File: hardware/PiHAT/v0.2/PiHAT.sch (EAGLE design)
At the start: 41 parts, among them U1 ATMEGA328P, U2 TSL2561, U3 OPA344, U4 MPL115A, U6 ADMP401, U7 SHT31-DIS, Y1 16MHZ

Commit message: Updated PiAQ HAT to v0.2
- Added LEDs on GPIO 05, 26
- Replaced IAQ Core with CCS811
- Added more thermal isolation and rerouted traces
- Minor silkscreen adjustments
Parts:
- removed IAQ-CORE: IAQ-CORE, IAQ-CORE:IAQ-CORE
- added LED_05, LED_26: (no value), adafruit:LEDCHIPLED_0805
- added R10, R2: 47, SparkFun-Resistors:RESISTOR0805-RES
- added R9: 100K, SparkFun-Passives:RESISTOR0805-RES
- added U$1: CCS811, CCS811:CCS811-I2C
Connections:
- new net N$1: LED_26.A, R2.1
- new net N$16: R9.2, U$1.ADDR
- new net N$6: LED_05.A, R10.1
- net GND: now also LED_05.C, LED_26.C, U$1.GND; no longer IAQ-CORE.GND
- net GPIO26: now also R2.2
- net GPIO5: now also R10.2
- net SCL: now also U$1.SCL; no longer IAQ-CORE.SCL
- net SDA: now also U$1.SDA; no longer IAQ-CORE.SDA
- net VCC: now also R9.1, U$1.VDD; no longer IAQ-CORE.VCC
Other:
- note added: "0x5B"
- note added: "v0.2 (October 2016)"
- note removed: "0x5A"
- note removed: "v0.1 (September 2016)"
- moved on the sheet: C5

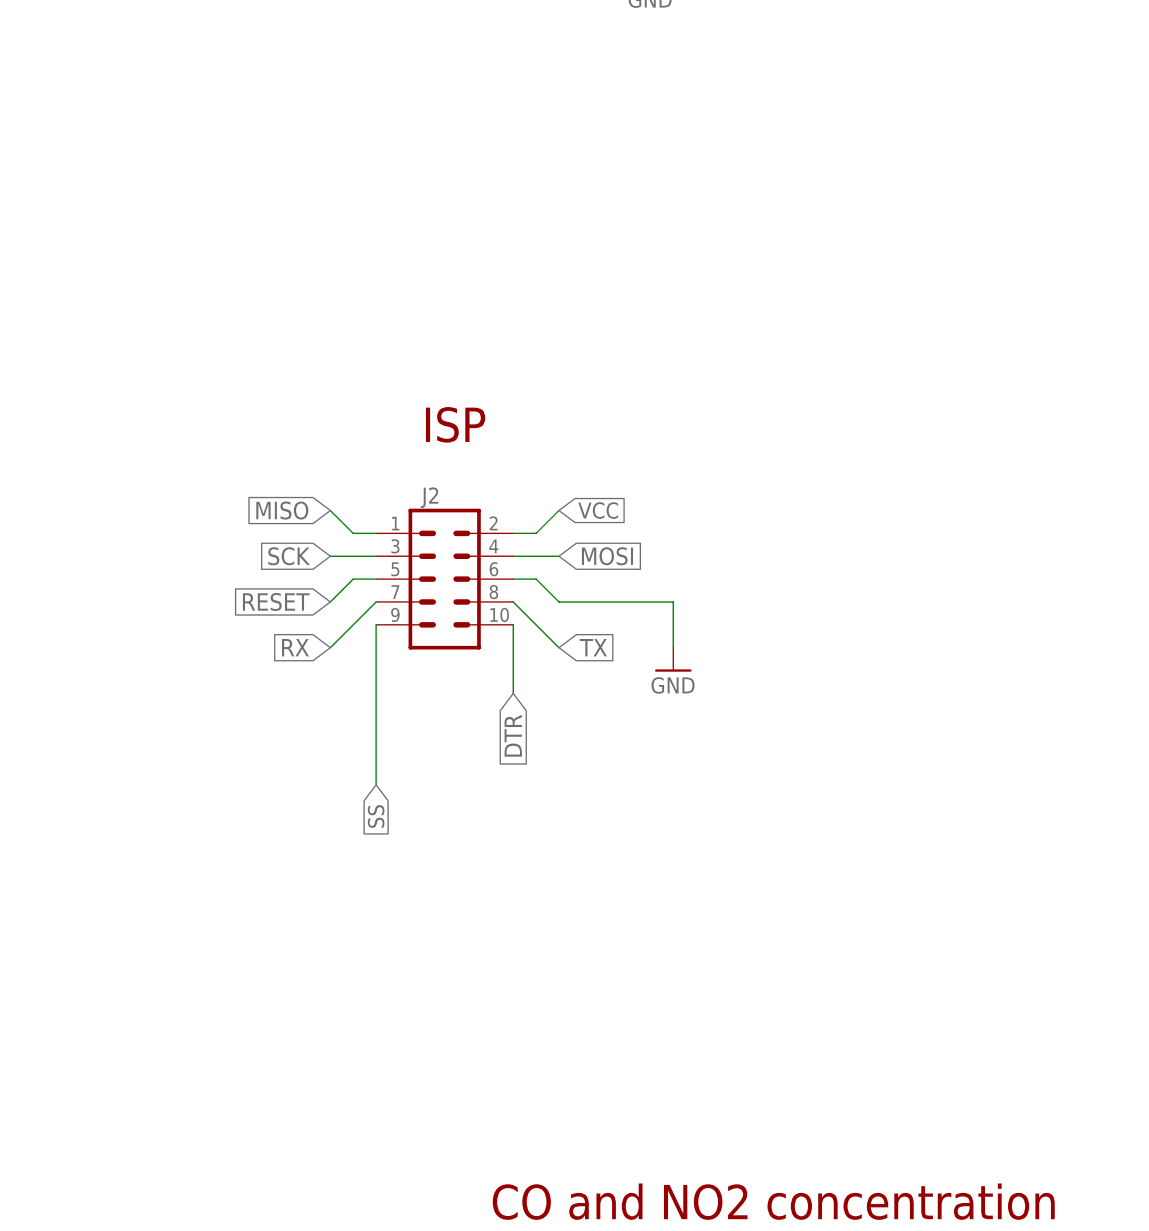
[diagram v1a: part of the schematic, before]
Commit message: Minor fixes to sensor board v0.6
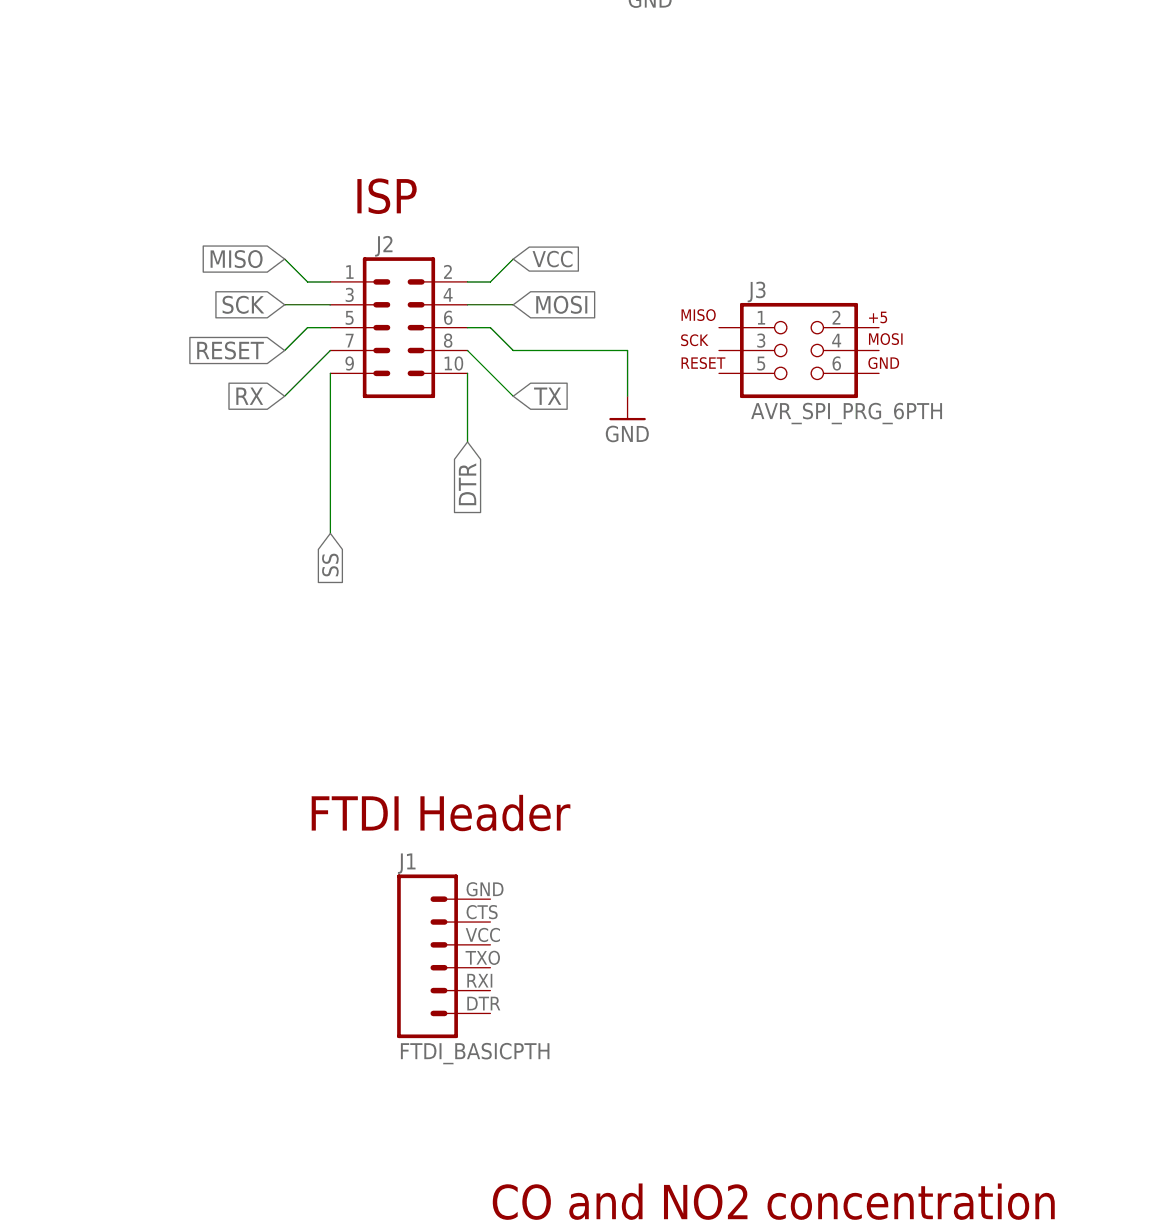
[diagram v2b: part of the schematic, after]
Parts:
- added J1: FTDI_BASICPTH, SparkFun-Connectors:FTDI_BASICPTH
- added J3: AVR_SPI_PRG_6PTH, SparkFun-Connectors:AVR_SPI_PRG_6PTH
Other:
- note added: "FTDI Header"
- moved on the sheet: J2
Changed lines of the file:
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@@
 <attribute name="OC_NEWARK" value="unknown"/>
 </part>
+<part name="J1" library="SparkFun-Connectors" deviceset="FTDI_BASIC" device="PTH"/>
+<part name="J3" library="SparkFun-Connectors" deviceset="AVR_SPI_PRG_6" device="PTH"/>
 </parts>
 <sheets>
@@
 <text x="447.04" y="-71.12" size="3.81" layer="94">Sound Intensity</text>
 <text x="426.72" y="17.78" size="3.81" layer="94">Temperature and Relative Humidity</text>
-<text x="185.42" y="5.08" size="3.81" layer="94">ISP</text>
+<text x="177.8" y="30.48" size="3.81" layer="94">ISP</text>
 <text x="193.04" y="-81.28" size="3.81" layer="94">CO and NO2 concentration</text>
 <text x="322.58" y="-132.08" size="5.08" layer="94" font="vector" ratio="20">CRT Labs</text>
@@
 <text x="467.36" y="-17.78" size="1.778" layer="97">0x44</text>
 <frame x1="104.14" y1="-167.64" x2="568.96" y2="165.1" columns="8" rows="5" layer="94"/>
+<text x="172.72" y="-38.1" size="3.81" layer="94">FTDI Header</text>
 </plain>
 <instances>
@@
 </instance>
 <instance part="SUPPLY11" gate="G$1" x="426.72" y="132.08"/>
-<instance part="J2" gate="G$1" x="187.96" y="-10.16">
-<attribute name="DIGIKEY#" x="187.96" y="-10.16" size="1.778" layer="96" display="off"/>
+<instance part="J2" gate="G$1" x="182.88" y="17.78">
+<attribute name="DIGIKEY#" x="182.88" y="17.78" size="1.778" layer="96" display="off"/>
 </instance>
 <instance part="U4" gate="G$1" x="325.12" y="109.22">
@@
 </instance>
 <instance part="SUPPLY12" gate="G$1" x="289.56" y="119.38"/>
-<instance part="GND6" gate="1" x="213.36" y="-20.32"/>
+<instance part="GND6" gate="1" x="208.28" y="7.62"/>
 <instance part="MICS4514" gate="G$1" x="254" y="-99.06"/>
 <instance part="R14" gate="G$1" x="223.52" y="-111.76" rot="R90">
@@
 <attribute name="DIGIKEY#" x="129.54" y="73.66" size="1.778" layer="96" rot="R270" display="off"/>
 </instance>
+<instance part="J1" gate="G$1" x="187.96" y="-53.34"/>
+<instance part="J3" gate="G$1" x="226.06" y="15.24"/>
 </instances>
 <busses>
@@
 <segment>
 <pinref part="J2" gate="G$1" pin="6"/>
-<wire x1="195.58" y1="-10.16" x2="198.12" y2="-10.16" width="0.1524" layer="91"/>
-<wire x1="198.12" y1="-10.16" x2="200.66" y2="-12.7" width="0.1524" layer="91"/>
-<wire x1="200.66" y1="-12.7" x2="213.36" y2="-12.7" width="0.1524" layer="91"/>
-<wire x1="213.36" y1="-12.7" x2="213.36" y2="-17.78" width="0.1524" layer="91"/>
+<wire x1="190.5" y1="17.78" x2="193.04" y2="17.78" width="0.1524" layer="91"/>
+<wire x1="193.04" y1="17.78" x2="195.58" y2="15.24" width="0.1524" layer="91"/>
+<wire x1="195.58" y1="15.24" x2="208.28" y2="15.24" width="0.1524" layer="91"/>
+<wire x1="208.28" y1="15.24" x2="208.28" y2="10.16" width="0.1524" layer="91"/>
 <pinref part="GND6" gate="1" pin="GND"/>
 </segment>
@@
 <segment>
 <pinref part="J2" gate="G$1" pin="2"/>
-<wire x1="195.58" y1="-5.08" x2="198.12" y2="-5.08" width="0.1524" layer="91"/>
-<wire x1="198.12" y1="-5.08" x2="200.66" y2="-2.54" width="0.1524" layer="91"/>
-<label x="200.66" y="-2.54" size="1.778" layer="95" xref="yes"/>
+<wire x1="190.5" y1="22.86" x2="193.04" y2="22.86" width="0.1524" layer="91"/>
+<wire x1="193.04" y1="22.86" x2="195.58" y2="25.4" width="0.1524" layer="91"/>
+<label x="195.58" y="25.4" size="1.778" layer="95" xref="yes"/>
 </segment>
 <segment>
@@
 <segment>
 <pinref part="J2" gate="G$1" pin="1"/>
-<wire x1="180.34" y1="-5.08" x2="177.8" y2="-5.08" width="0.1524" layer="91"/>
-<wire x1="177.8" y1="-5.08" x2="175.26" y2="-2.54" width="0.1524" layer="91"/>
-<label x="175.26" y="-2.54" size="1.9304" layer="95" rot="R180" xref="yes"/>
+<wire x1="175.26" y1="22.86" x2="172.72" y2="22.86" width="0.1524" layer="91"/>
+<wire x1="172.72" y1="22.86" x2="170.18" y2="25.4" width="0.1524" layer="91"/>
+<label x="170.18" y="25.4" size="1.9304" layer="95" rot="R180" xref="yes"/>
 </segment>
 </net>
@@
 <segment>
 <pinref part="J2" gate="G$1" pin="3"/>
-<wire x1="180.34" y1="-7.62" x2="175.26" y2="-7.62" width="0.1524" layer="91"/>
-<label x="175.26" y="-7.62" size="1.9304" layer="95" rot="R180" xref="yes"/>
+<wire x1="175.26" y1="20.32" x2="170.18" y2="20.32" width="0.1524" layer="91"/>
+<label x="170.18" y="20.32" size="1.9304" layer="95" rot="R180" xref="yes"/>
 </segment>
 </net>
@@
 <segment>
 <pinref part="J2" gate="G$1" pin="5"/>
-<wire x1="180.34" y1="-10.16" x2="177.8" y2="-10.16" width="0.1524" layer="91"/>
-<wire x1="177.8" y1="-10.16" x2="175.26" y2="-12.7" width="0.1524" layer="91"/>
-<label x="175.26" y="-12.7" size="1.9304" layer="95" rot="R180" xref="yes"/>
+<wire x1="175.26" y1="17.78" x2="172.72" y2="17.78" width="0.1524" layer="91"/>
+<wire x1="172.72" y1="17.78" x2="170.18" y2="15.24" width="0.1524" layer="91"/>
+<label x="170.18" y="15.24" size="1.9304" layer="95" rot="R180" xref="yes"/>
 </segment>
 </net>
@@
 <segment>
 <pinref part="J2" gate="G$1" pin="4"/>
-<wire x1="195.58" y1="-7.62" x2="200.66" y2="-7.62" width="0.1524" layer="91"/>
-<label x="200.66" y="-7.62" size="1.9304" layer="95" xref="yes"/>
+<wire x1="190.5" y1="20.32" x2="195.58" y2="20.32" width="0.1524" layer="91"/>
+<label x="195.58" y="20.32" size="1.9304" layer="95" xref="yes"/>
 </segment>
 </net>
@@
 <segment>
 <pinref part="J2" gate="G$1" pin="10"/>
-<wire x1="195.58" y1="-15.24" x2="195.58" y2="-22.86" width="0.1524" layer="91"/>
-<label x="195.58" y="-22.86" size="1.9304" layer="95" rot="R270" xref="yes"/>
+<wire x1="190.5" y1="12.7" x2="190.5" y2="5.08" width="0.1524" layer="91"/>
+<label x="190.5" y="5.08" size="1.9304" layer="95" rot="R270" xref="yes"/>
 </segment>
 </net>
@@
 <segment>
 <pinref part="J2" gate="G$1" pin="7"/>
-<wire x1="180.34" y1="-12.7" x2="175.26" y2="-17.78" width="0.1524" layer="91"/>
-<label x="175.26" y="-17.78" size="1.9304" layer="95" rot="R180" xref="yes"/>
+<wire x1="175.26" y1="15.24" x2="170.18" y2="10.16" width="0.1524" layer="91"/>
+<label x="170.18" y="10.16" size="1.9304" layer="95" rot="R180" xref="yes"/>
 </segment>
 <segment>
@@
 <segment>
 <pinref part="J2" gate="G$1" pin="8"/>
-<wire x1="195.58" y1="-12.7" x2="200.66" y2="-17.78" width="0.1524" layer="91"/>
-<label x="200.66" y="-17.78" size="1.9304" layer="95" xref="yes"/>
+<wire x1="190.5" y1="15.24" x2="195.58" y2="10.16" width="0.1524" layer="91"/>
+<label x="195.58" y="10.16" size="1.9304" layer="95" xref="yes"/>
 </segment>
 <segment>
@@
 <segment>
 <pinref part="J2" gate="G$1" pin="9"/>
-<wire x1="180.34" y1="-15.24" x2="180.34" y2="-33.02" width="0.1524" layer="91"/>
-<label x="180.34" y="-33.02" size="1.778" layer="95" rot="R270" xref="yes"/>
-</segment>
-</net>
+<wire x1="175.26" y1="12.7" x2="175.26" y2="-5.08" width="0.1524" layer="91"/>
+<label x="175.26" y="-5.08" size="1.778" layer="95" rot="R270" xref="yes"/>
+</segment>
+</net>

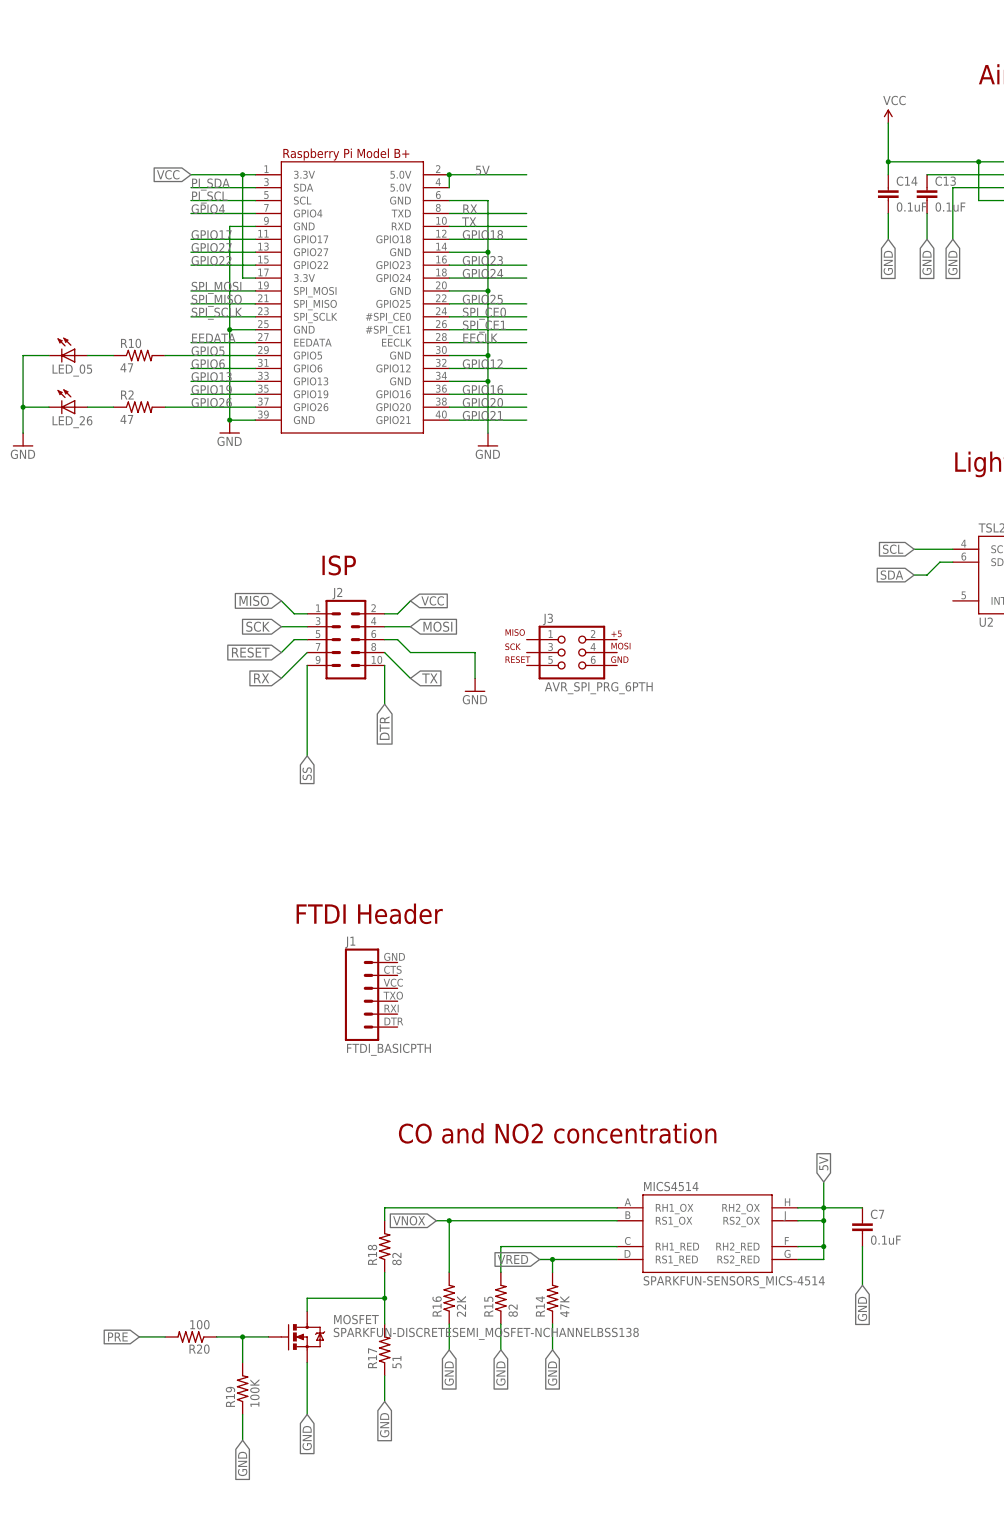
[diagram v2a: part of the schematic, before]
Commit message: Added FTDI headers to Pi HAT, separated ISP headers
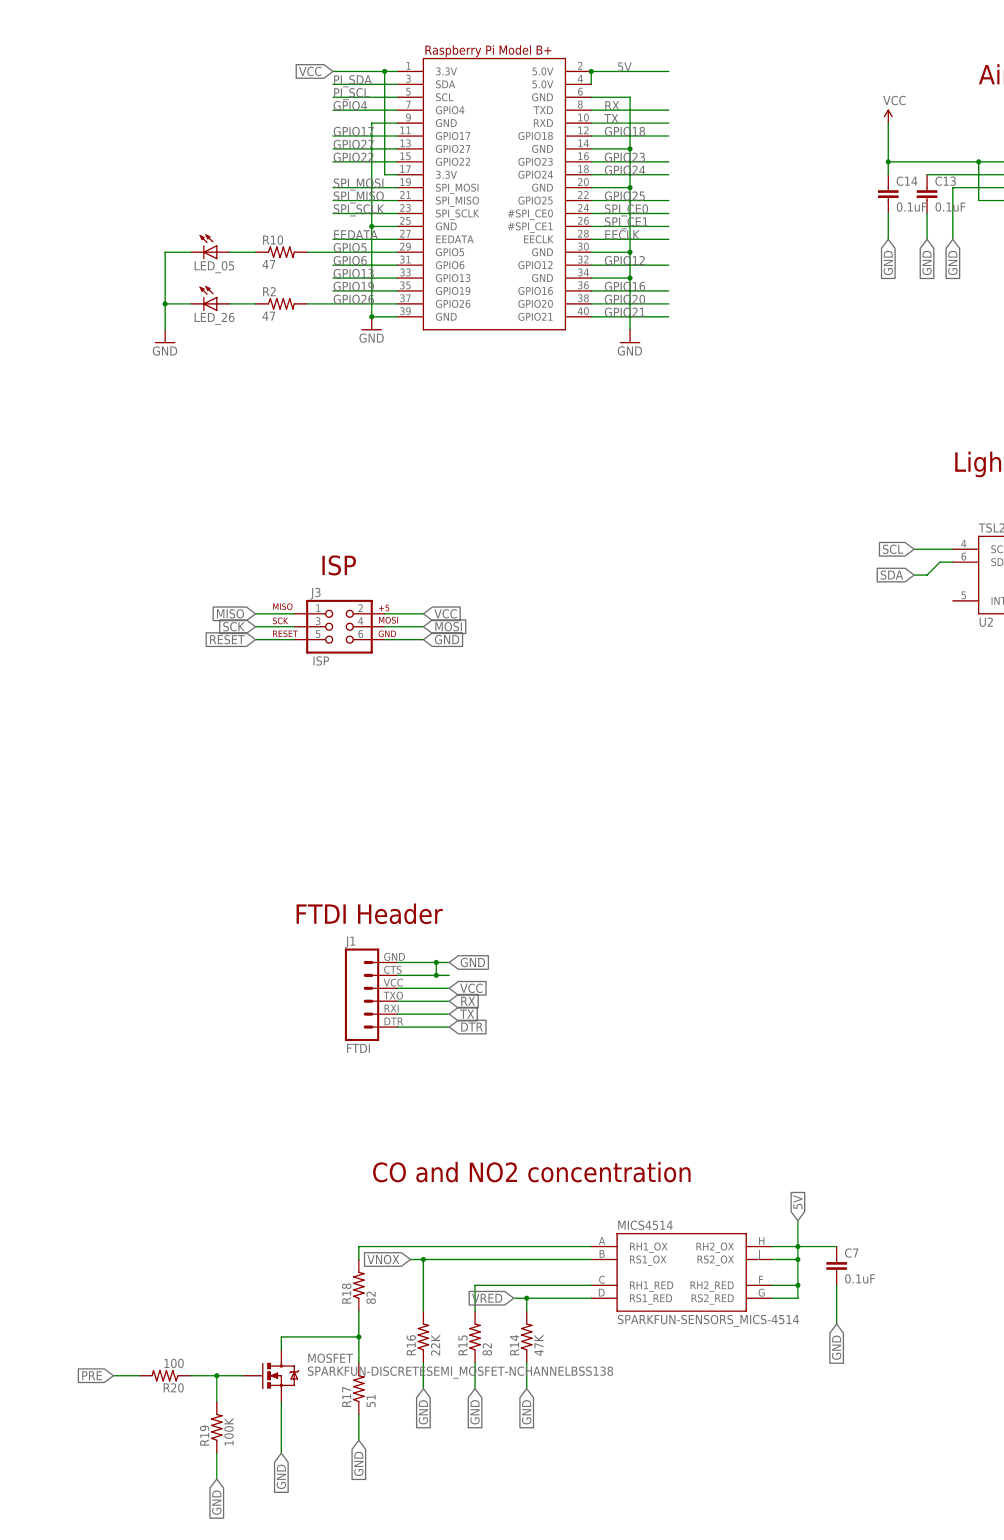
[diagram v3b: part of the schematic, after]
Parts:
- removed J2: (no value), SparkFun-Connectors:M05X2PTH
- J1: value FTDI_BASICPTH -> FTDI
- J3: value AVR_SPI_PRG_6PTH -> ISP
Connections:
- net DTR: now also J1.1; no longer J2.10
- net GND: now also J1.5, J1.6, J3.6; no longer J2.6
- net MISO: now also J3.1; no longer J2.1
- net MOSI: now also J3.4; no longer J2.4
- net RESET: now also J3.5; no longer J2.5
- net RX: now also J1.3; no longer J2.7
- net SCK: now also J3.3; no longer J2.3
- net SS: no longer J2.9
- net TX: now also J1.2; no longer J2.8
- net VCC: now also J1.4, J3.2; no longer J2.2
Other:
- moved on the sheet: C7, J3, LED_05, LED_26, MICS4514, MOSFET, R10, R14, R15, R16, R17, R18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

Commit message: adding MPN to v2 schematics
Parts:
- C10, C12, C13, C14, C15, C3, C4, C5, C7: MPN (none) -> CC0603KRX7R7BB104
- C2: MPN (none) -> CC0805JRNPO9BN101
- C8: MPN (none) -> CC0805KKX5R8BB475
- C9: MPN (none) -> CC0805KKX7R7BB105
- J1: MPN (none) -> FT231XS-R
- LED_05, LED_26: MPN (none) -> LY L29K-H1K2-26-Z
- MOSFET: MPN (none) -> BSS138-7-F
- R1, R13, R5, R6, R7: MPN (none) -> RC0805JR-0710KL
- R10, R2, R4: MPN (none) -> RC0805JR-0747RL
- R14: MPN (none) -> ESR10EZPJ473
- R15, R18: MPN (none) -> CRCW080582R0FKEA
- R16: MPN (none) -> RC0805JR-0722KL
- R17: MPN (none) -> ESR10EZPJ510
- R19, R8, R9: MPN (none) -> RC0805FR-07100KL
- R20: MPN (none) -> RC0805FR-07100RL
- R3: MPN (none) -> RT0805BRD071K5L
- RESET: MPN (none) -> PTS525SM15SMTR2 LFS
- U3: MPN (none) -> OPA344NA/3K
- U4: MPN (none) -> MPL115A2
- U6: MPN (none) -> INMP401ACEZ-R7
- Y1: MPN (none) -> CSTCE16M0V53-R0; OC_NEWARK unknown -> (none)
